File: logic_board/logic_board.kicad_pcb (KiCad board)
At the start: 4 copper layers, 80 x 30 mm, 66 parts, among them J1 SWD, J2 Audio In, J3 SJ2-3595X-SMT, J4 Amphenol 124015, J5 Batt, J6 Serial, SW1 TL3315NF160Q, SW2 TL3315NF160Q, SW3 TL3315NF160Q, SW4 TL3315NF160Q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

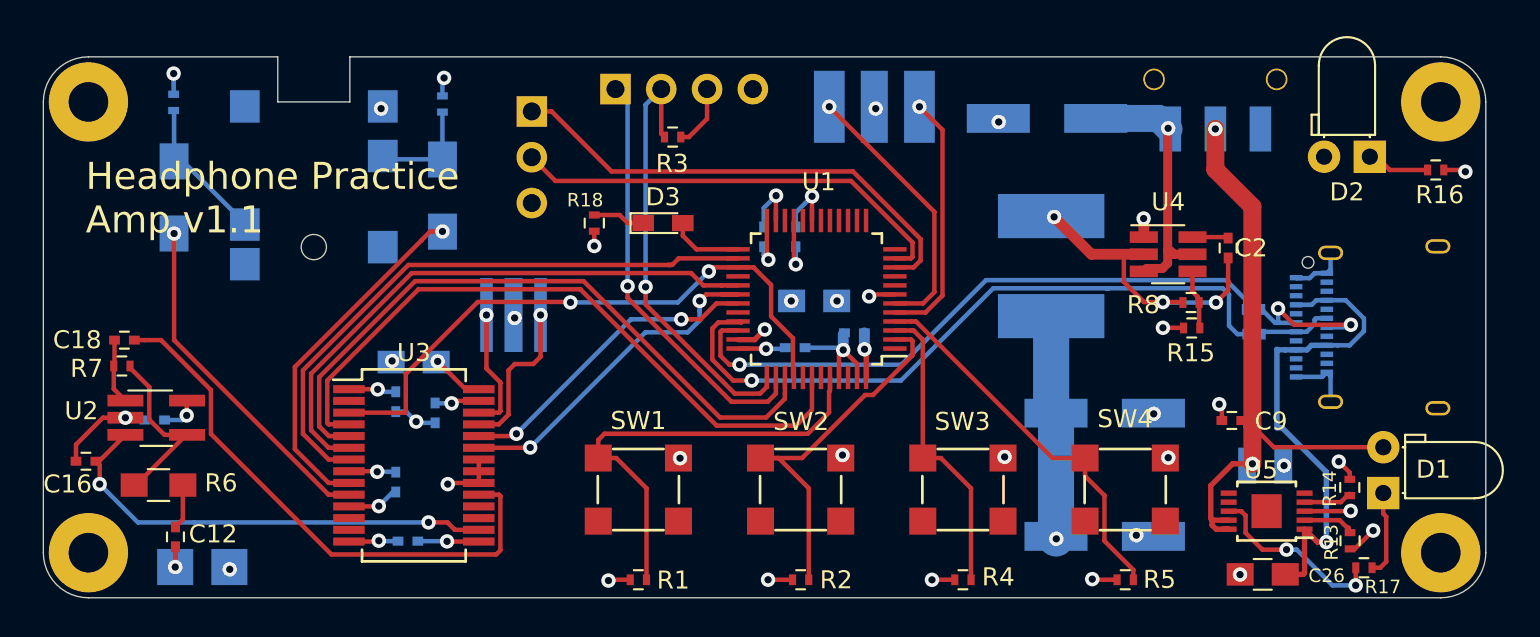
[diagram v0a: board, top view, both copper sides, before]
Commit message: Remove external pullups.
The chip already has internal ones.
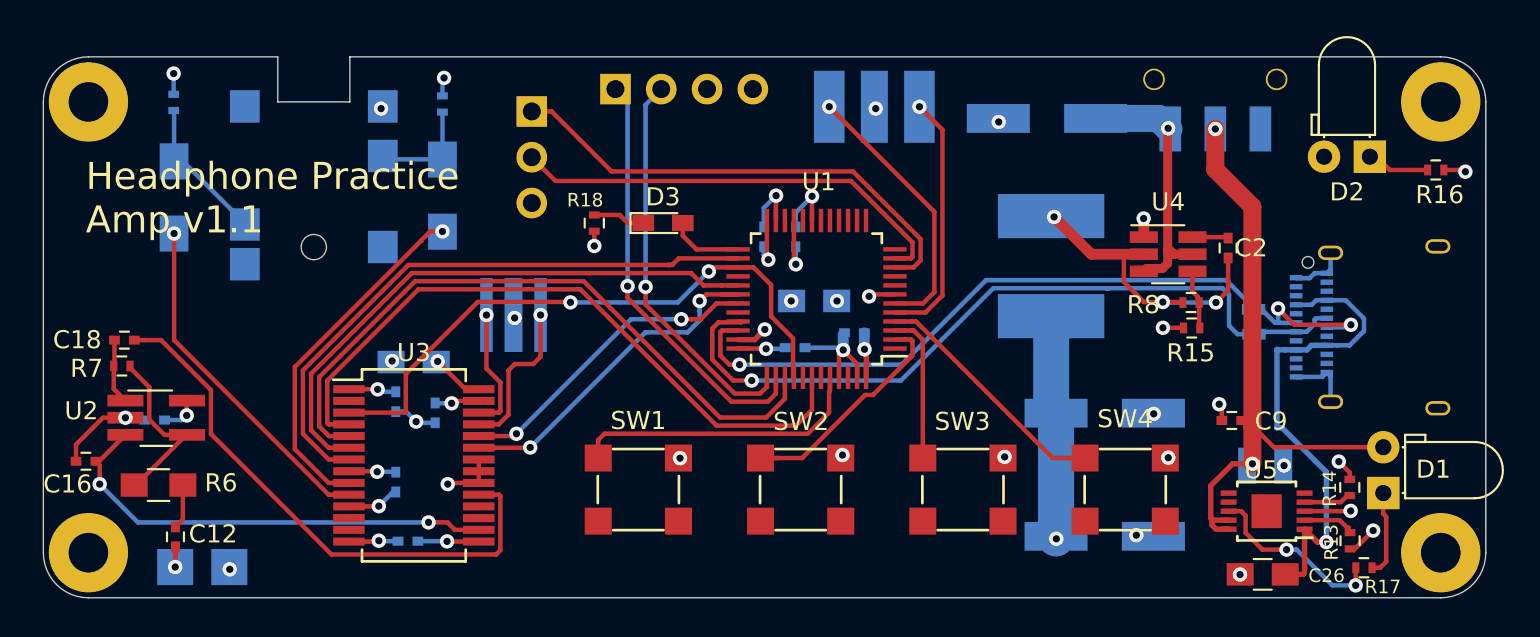
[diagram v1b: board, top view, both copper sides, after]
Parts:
- removed R1, R2, R4, R5: 10k, Resistors_SMD:R_0402
- removed R3: 100k, Resistors_SMD:R_0402
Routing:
- net +3V3: track 47.1 -> 38.3 mm, vias 17 -> 13
- net SW3: track 16.8 -> 8.32 mm
- net SW1: track 24.8 -> 16.4 mm
- net SW4: track 21.5 -> 13.7 mm
- net SW2: track 21.0 -> 13.6 mm
- net Net-(J1-Pad2): track 24.5 -> 21.8 mm

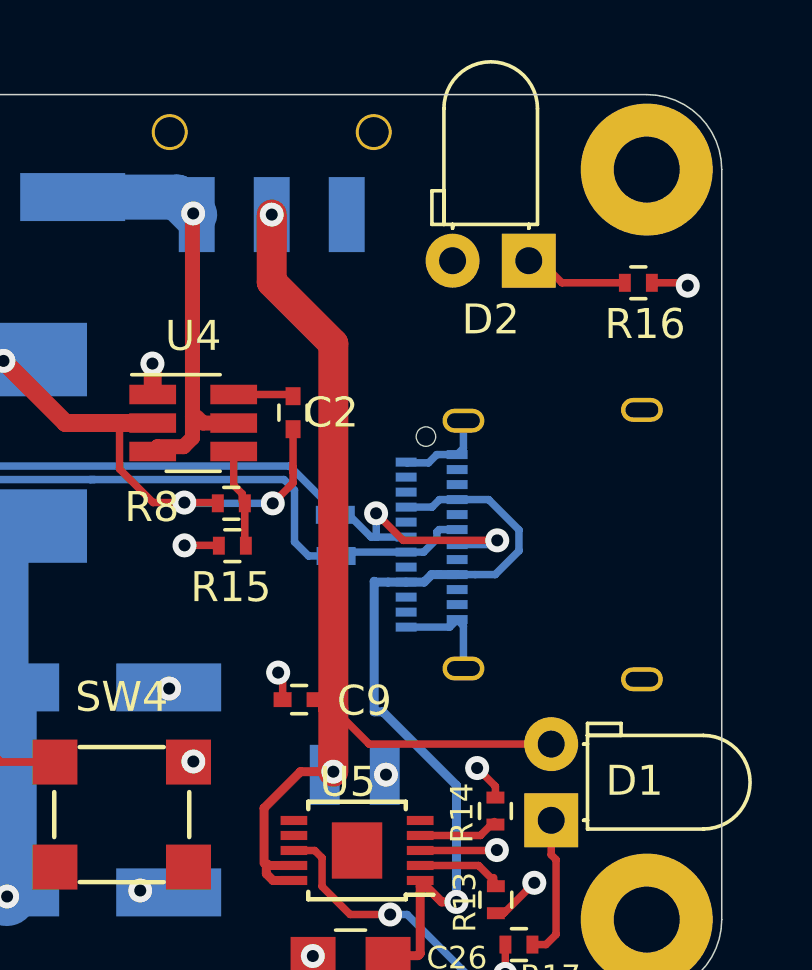
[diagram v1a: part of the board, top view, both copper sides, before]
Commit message: Add pulldown resistors on CC1 and CC2 pins to enable VBUS power
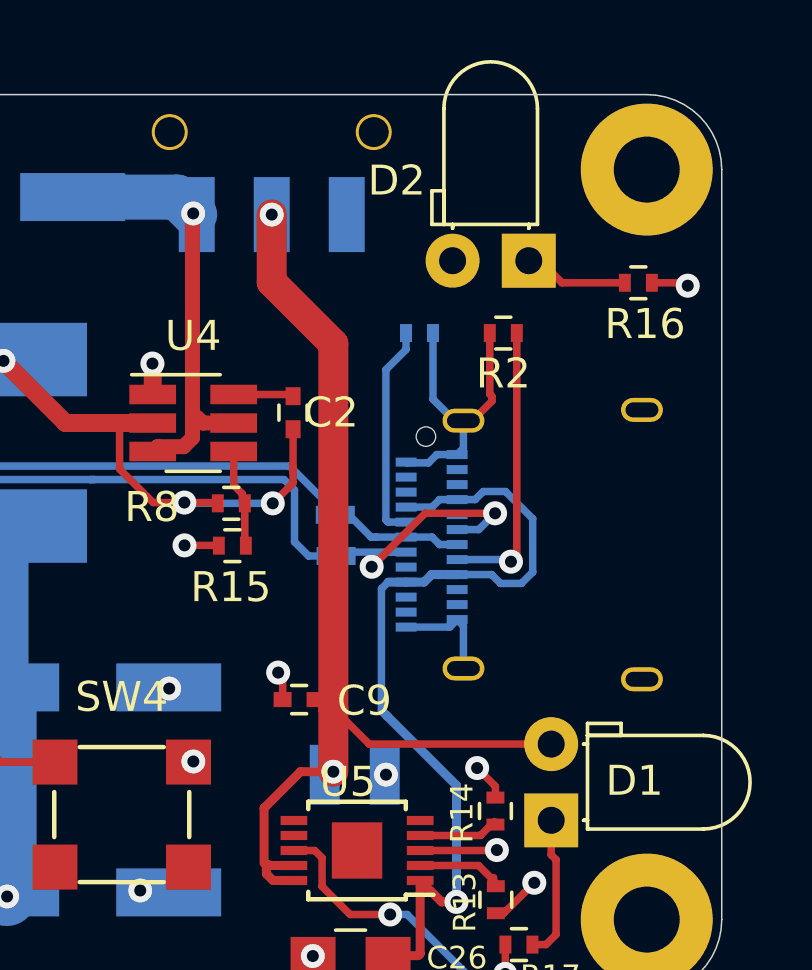
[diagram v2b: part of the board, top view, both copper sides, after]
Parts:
- added R1: 5.1k, Resistors_SMD:R_0402, B.Cu at (169.9, 108.0)
- added R2: 5.1k, Resistors_SMD:R_0402, F.Cu at (172.7, 108.0)
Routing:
- net Net-(J4-PadB5): track 0.00 -> 9.52 mm, vias 0 -> 1
- net Net-(J4-PadA5): track 0.00 -> 7.21 mm
- net GND: track 54.7 -> 61.9 mm
- net Net-(J4-PadA7): track 4.09 -> 9.63 mm, vias 0 -> 2
- net Net-(J4-PadA6): track 8.82 -> 4.02 mm, vias 2 -> 0
- net Net-(C26-Pad1): track 27.3 -> 28.8 mm

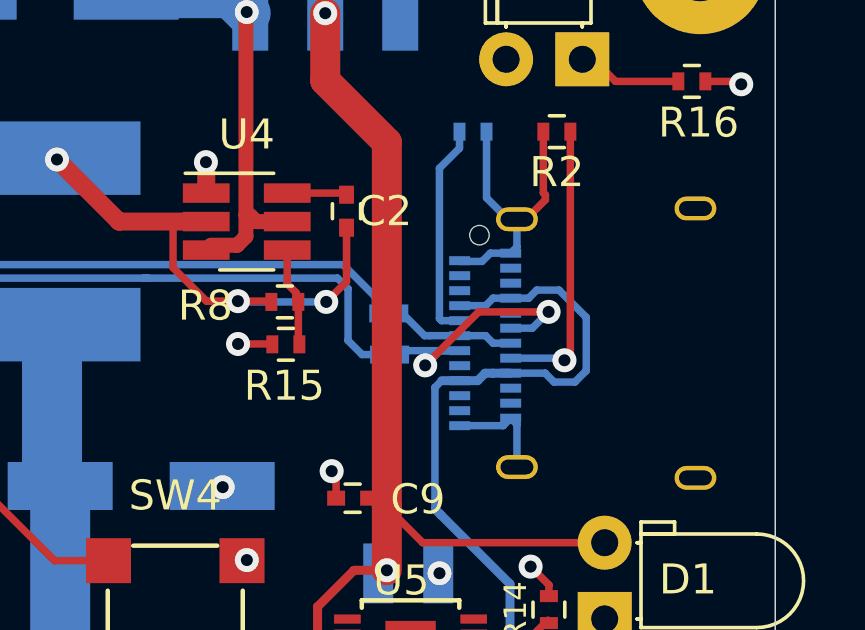
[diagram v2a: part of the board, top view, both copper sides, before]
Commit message: Remove USB series termination resistors
Page 179 of the datasheet states: "No external termination series
resistors are required on USB_PD P(D+) and USB_DM (D-); the matching
impedance is already included in the embedded driver." (There's a typo,
presumably they meant USB_DP).
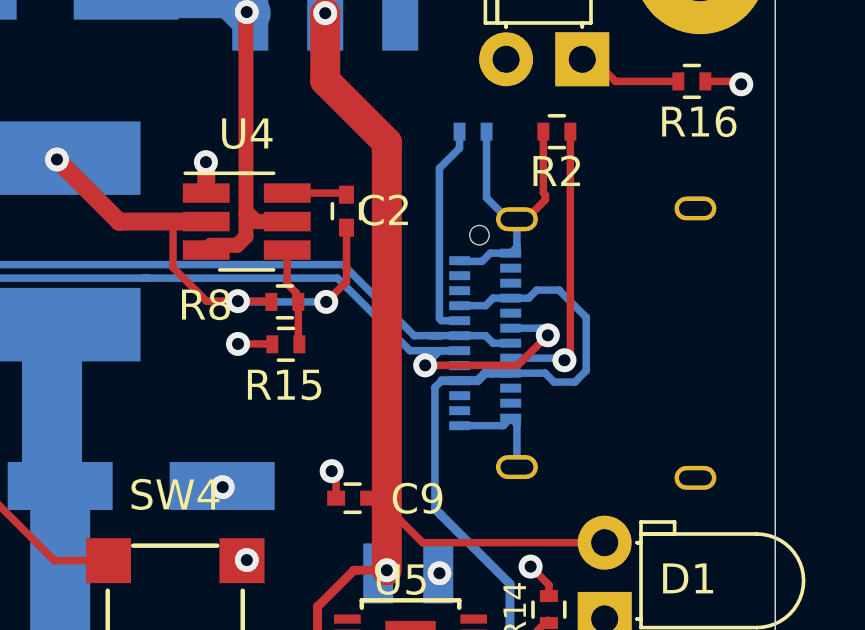
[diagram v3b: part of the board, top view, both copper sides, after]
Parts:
- removed R11, R12: 33, Resistors_SMD:R_0402
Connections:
- J4 pad A6: Net-(J4-PadA6) -> USB_DP
- J4 pad A7: Net-(J4-PadA7) -> USB_DM
- J4 pad B6: Net-(J4-PadA6) -> USB_DP
- J4 pad B7: Net-(J4-PadA7) -> USB_DM
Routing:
- net Net-(J4-PadA7): track 9.63 -> 0.00 mm, vias 2 -> 0
- net USB_DM: track 38.1 -> 47.2 mm, vias 1 -> 3
- net USB_DP: track 34.6 -> 39.6 mm
- net Net-(J4-PadA6): track 4.02 -> 0.00 mm

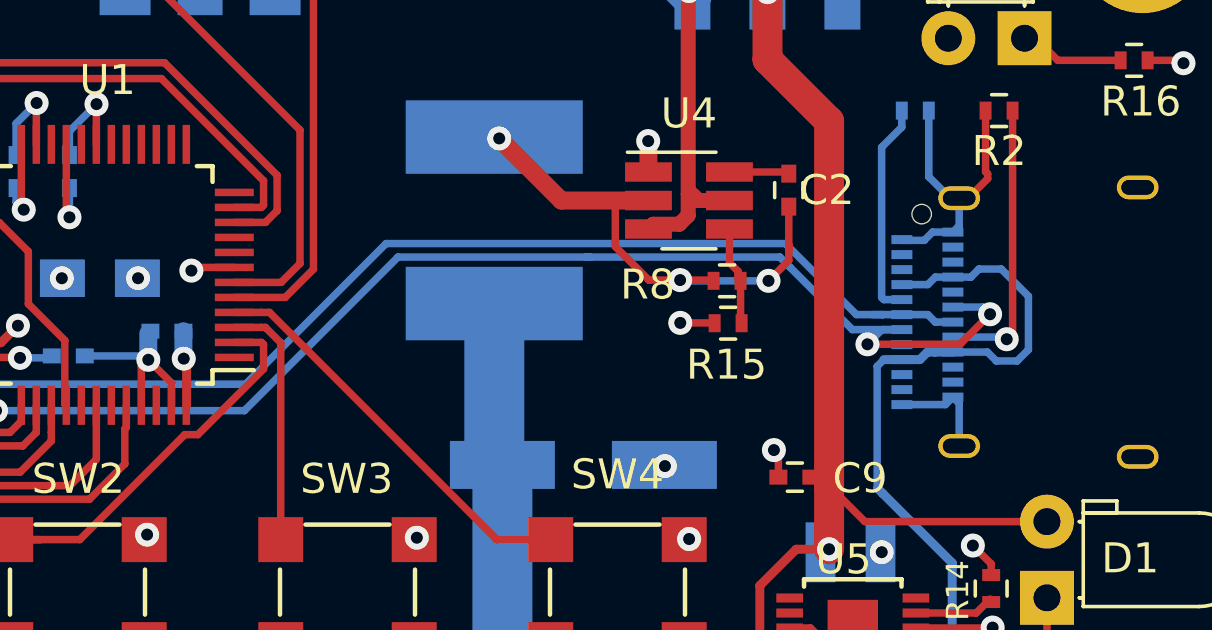
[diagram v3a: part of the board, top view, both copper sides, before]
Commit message: Connect VBAT to VDD
From AN5096, "If no external battery is used in the application, it is recommended
to connect VBAT externally to VDD."
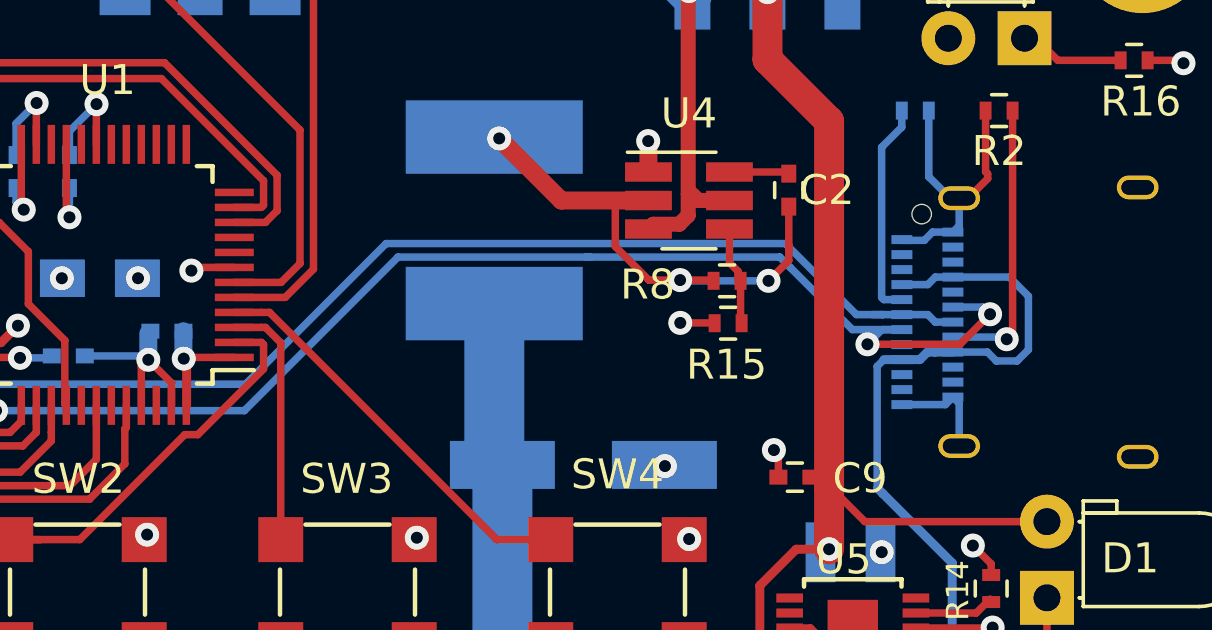
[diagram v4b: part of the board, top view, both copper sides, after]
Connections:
- U1 pad 1: Net-(U1-Pad1) -> +3V3
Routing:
- net +3V3: track 38.3 -> 40.0 mm

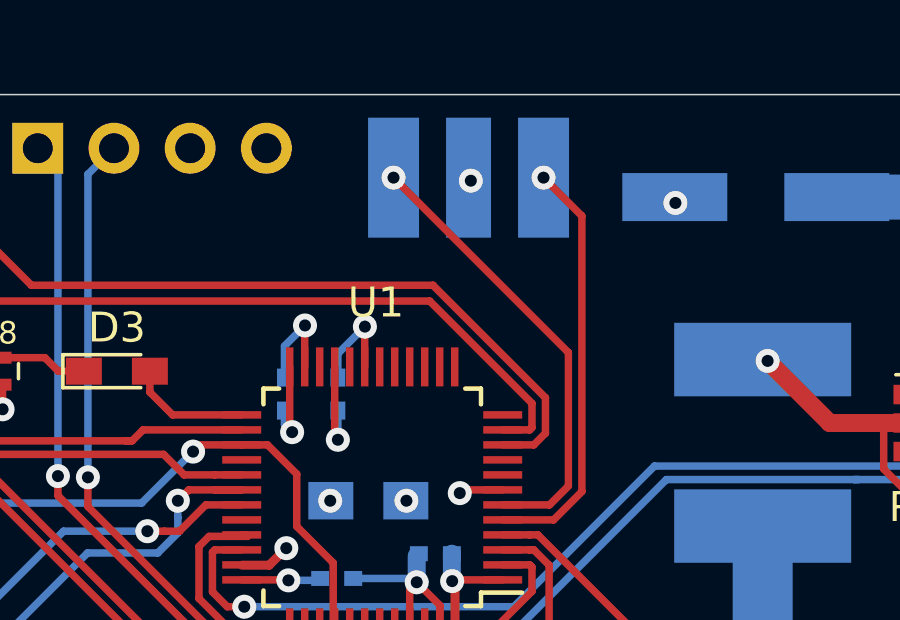
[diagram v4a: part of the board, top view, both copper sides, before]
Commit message: Swap MCU resonator so the input/outputs are connected correctly.
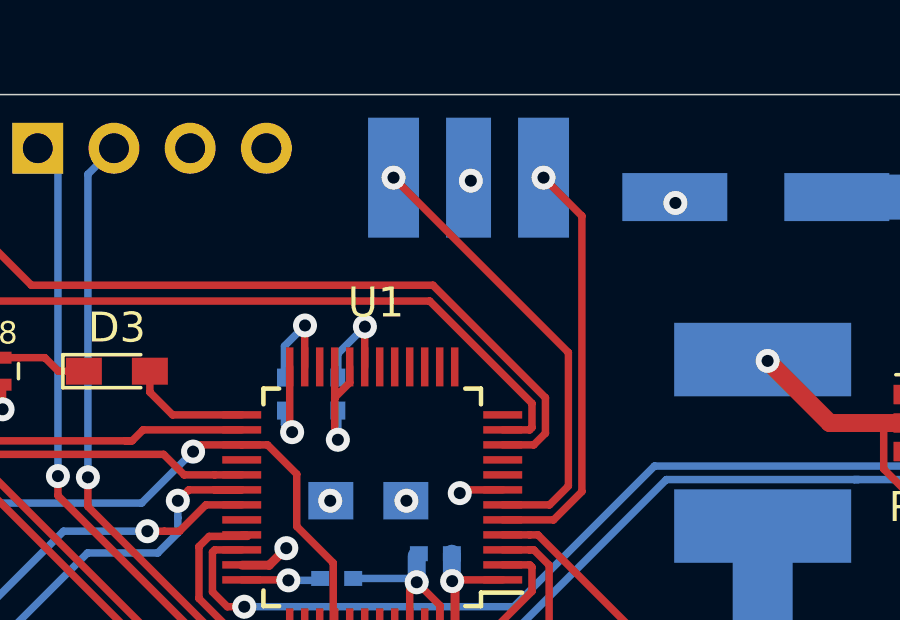
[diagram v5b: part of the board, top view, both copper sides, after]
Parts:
- turned Y1 to 0 degrees
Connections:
- U1 pad 20: Net-(U1-Pad20) -> +3V3
- Y1 pad 1: Net-(U1-Pad5) -> Net-(U1-Pad6)
- Y1 pad 3: Net-(U1-Pad6) -> Net-(U1-Pad5)
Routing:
- net +3V3: track 40.0 -> 41.2 mm
